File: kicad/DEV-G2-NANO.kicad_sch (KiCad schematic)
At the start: 0 parts

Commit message: added MIMXRT1171DVMAB symbol to project
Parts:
- added C1, C10, C11, C12, C13, C2, C3, C4, C5, C6: ???, symbol Device:C_Small
- added C14, C16, C17, C7, C8: 100nF, symbol Device:C_Small
- added C15: 1μF, symbol Device:C_Small
- added C9: 2.2μF, symbol Device:C_Small
- added D1, D2: ???, symbol Device:D_Small
- added J1: Micro_SD_Card, symbol Connector:Micro_SD_Card
- added J2: USB1, symbol Connector_Generic:Conn_01x04
- added L1: 4.7μH, symbol Device:L_Small
- added R1, R2, R3, R4: 10kΩ, symbol Device:R_Small_US
- added U1: MIMXRT1171DVMAB, symbol project_symbols:MIMXRT1171DVMAB
- added Y1: 24MHz, symbol Device:Crystal_Small
- added Y2: 32.768kHz, symbol Device:Crystal_Small
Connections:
- new net: C16.1, C9.1, U1.U11 (NVCC_SNVS), U1.U14 (VDD_SNVS_ANA)
- new net: C15.1, R1.1, U1.P3 (DCDC_PSWITCH)
- new net: R3.1, U1.F10 (VDD_MIPI_1P0)
- new net: C13.2, U1.U13 (RTC_XTALO), Y2.1
- new net: C12.2, U1.T13 (RTC_XTALI), Y2.2
- new net: D1.1 (K), D2.1 (K), U1.U12 (VDD_SNVS_IN)
- new net: J2.1 (Pin_1), U1.D17 (USB1_VBUS)
- new net: J2.2 (Pin_2), U1.E16 (USB1_DN)
- new net: J2.3 (Pin_3), U1.E17 (USB1_DP)
- new net: C11.2, U1.U16 (XTALI), Y1.1
- new net: C14.1, U1.P12 (VDD_LPSR_ANA)
- new net: J1.2 (DAT3/CD), U1.A16 (GPIO_SD_B1_05)
- new net: J1.1 (DAT2), U1.B15 (GPIO_SD_B1_04)
- new net: J1.3 (CMD), U1.B16 (GPIO_SD_B1_00)
- new net: J1.8 (DAT1), U1.B17 (GPIO_SD_B1_03)
- new net: J1.7 (DAT0), U1.C15 (GPIO_SD_B1_02)
- new net: J1.5 (CLK), U1.D15 (GPIO_SD_B1_01)
- new net: R2.1, U1.F9 (VDD_MIPI_1P8)
- new net: C7.1, U1.N11 (VDDA_1P0)
- new net: R4.1, U1.N4 (DCDC_MODE)
- new net: C8.1, U1.P11 (VDD_LPSR_DIG)
- new net: C17.1, U1.T14 (VDD_SNVS_DIG)
- new net: C10.2, U1.T16 (XTALO), Y1.2
- new net: L1.2, U1.T3 (DCDC_LP), U1.U3 (DCDC_LP)
- new net: L1.1, U1.T4 (DCDC_LN), U1.U4 (DCDC_LN)
- new net +1V0: C4.1, C5.1, C6.1, U1.H10 (VDD_SOC_IN), U1.H8 (VDD_SOC_IN), U1.H9 (VDD_SOC_IN), U1.J10 (VDD_SOC_IN), U1.J8 (VDD_SOC_IN), U1.J9 (VDD_SOC_IN), U1.K10 (VDD_SOC_IN), U1.K8 (DCDC_DIG), U1.K9 (DCDC_DIG), U1.L7 (DCDC_DIG_SENSE), U1.L8 (DCDC_DIG)
- new net +1V8: C1.1, C2.1, C3.1, U1.G16 (ADC_VREFH), U1.H12 (VDD_USB_1P8), U1.K15 (VDDA_ADC_1P8), U1.M11 (VDDA_1P8_IN), U1.M6 (DCDC_ANA_SENSE), U1.M7 (DCDC_ANA), U1.M8 (DCDC_ANA)
- new net +3V3: D1.2 (A), J1.4 (VDD), R1.2, U1.D12 (NVCC_DISP1), U1.D14 (NVCC_SD1), U1.E7 (NVCC_DISP2), U1.F6 (NVCC_EMC1), U1.F7 (NVCC_EMC1), U1.G12 (VDD_USB_3P3), U1.G13 (NVCC_SD2), U1.G6 (NVCC_EMC1), U1.H6 (NVCC_EMC2), U1.J13 (VDDA_ADC_3P3), U1.J6 (NVCC_EMC2), U1.L5 (DCDC_IN_Q), U1.M12 (NVCC_GPIO), U1.M5 (DCDC_IN), U1.N5 (DCDC_IN), U1.P7 (NVCC_LPSR), U1.R12 (VDD_LPSR_IN)
- new net GND: C1.2, C10.1, C11.1, C12.1, C13.1, C14.2, C15.2, C16.2, C17.2, C2.2, C3.2, C4.2, C5.2, C6.2, C7.2, C8.2, C9.2, J1.6 (VSS), J2.4 (Pin_4), R2.2, R3.2, R4.2, U1.A1 (VSS), U1.A17 (VSS), U1.B7 (VSS), U1.C10 (VSS), U1.C12 (VSS), U1.C14 (VSS), U1.C8 (VSS), U1.D4 (VSS), U1.F11 (VSS), U1.F12 (VSS), U1.F13 (VSS), U1.G10 (VSS), U1.G11 (VSS), U1.G15 (VSS), U1.G3 (VSS), U1.G7 (VSS), U1.G8 (VSS), U1.G9 (VSS), U1.H11 (VSS), U1.H7 (VSS), U1.J11 (VSS), U1.J7 (VSS), U1.K11 (VSS), U1.K6 (DCDC_GND), U1.K7 (DCDC_GND), U1.L10 (VSS), U1.L11 (VSS), U1.L15 (VSS), U1.L3 (VSS), U1.L6 (DCDC_GND), U1.P14 (VSS), U1.P4 (VSS), U1.R4 (VSS), U1.R7 (VSS), U1.T11 (TEST_MODE), U1.T12 (VSS), U1.U1 (VSS), U1.U17 (VSS)
- new net GNDA: J1.SH (SHIELD)
- new net POR_B: U1.T10 (POR_B)
- new net VBAT: D2.2 (A)
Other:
- added sheet Disclaimer (disclaimer.kicad_sch)
- note added: "Notes ----- * Since the POR_B pin needs 1.8V logic, it might make sense to power the MKL26Z128VFM4 at 1.8V. This would require setting the MIMXRT117x's UART bank to 1.8V as well..."
- note added: "Solder male header and use StarTech USBMBADAPT adapter (or similar)"
- note added: "TODO ---- 1. Review power sequence 2. Bypass capacitors 3. Where does VBAT come from? 4. GNDA needs coupling to GND"
- note added: "TODO: Where to route this 1.8V DAC?"
- note added: "\ | | \ TODO: / IMU & Magnetometer | | /"
- note added: "\ | | \ TODO: / RTMC Core | | /"
- note added: "\ | | \ TODO: / Wi-Fi Companion IC | | /"

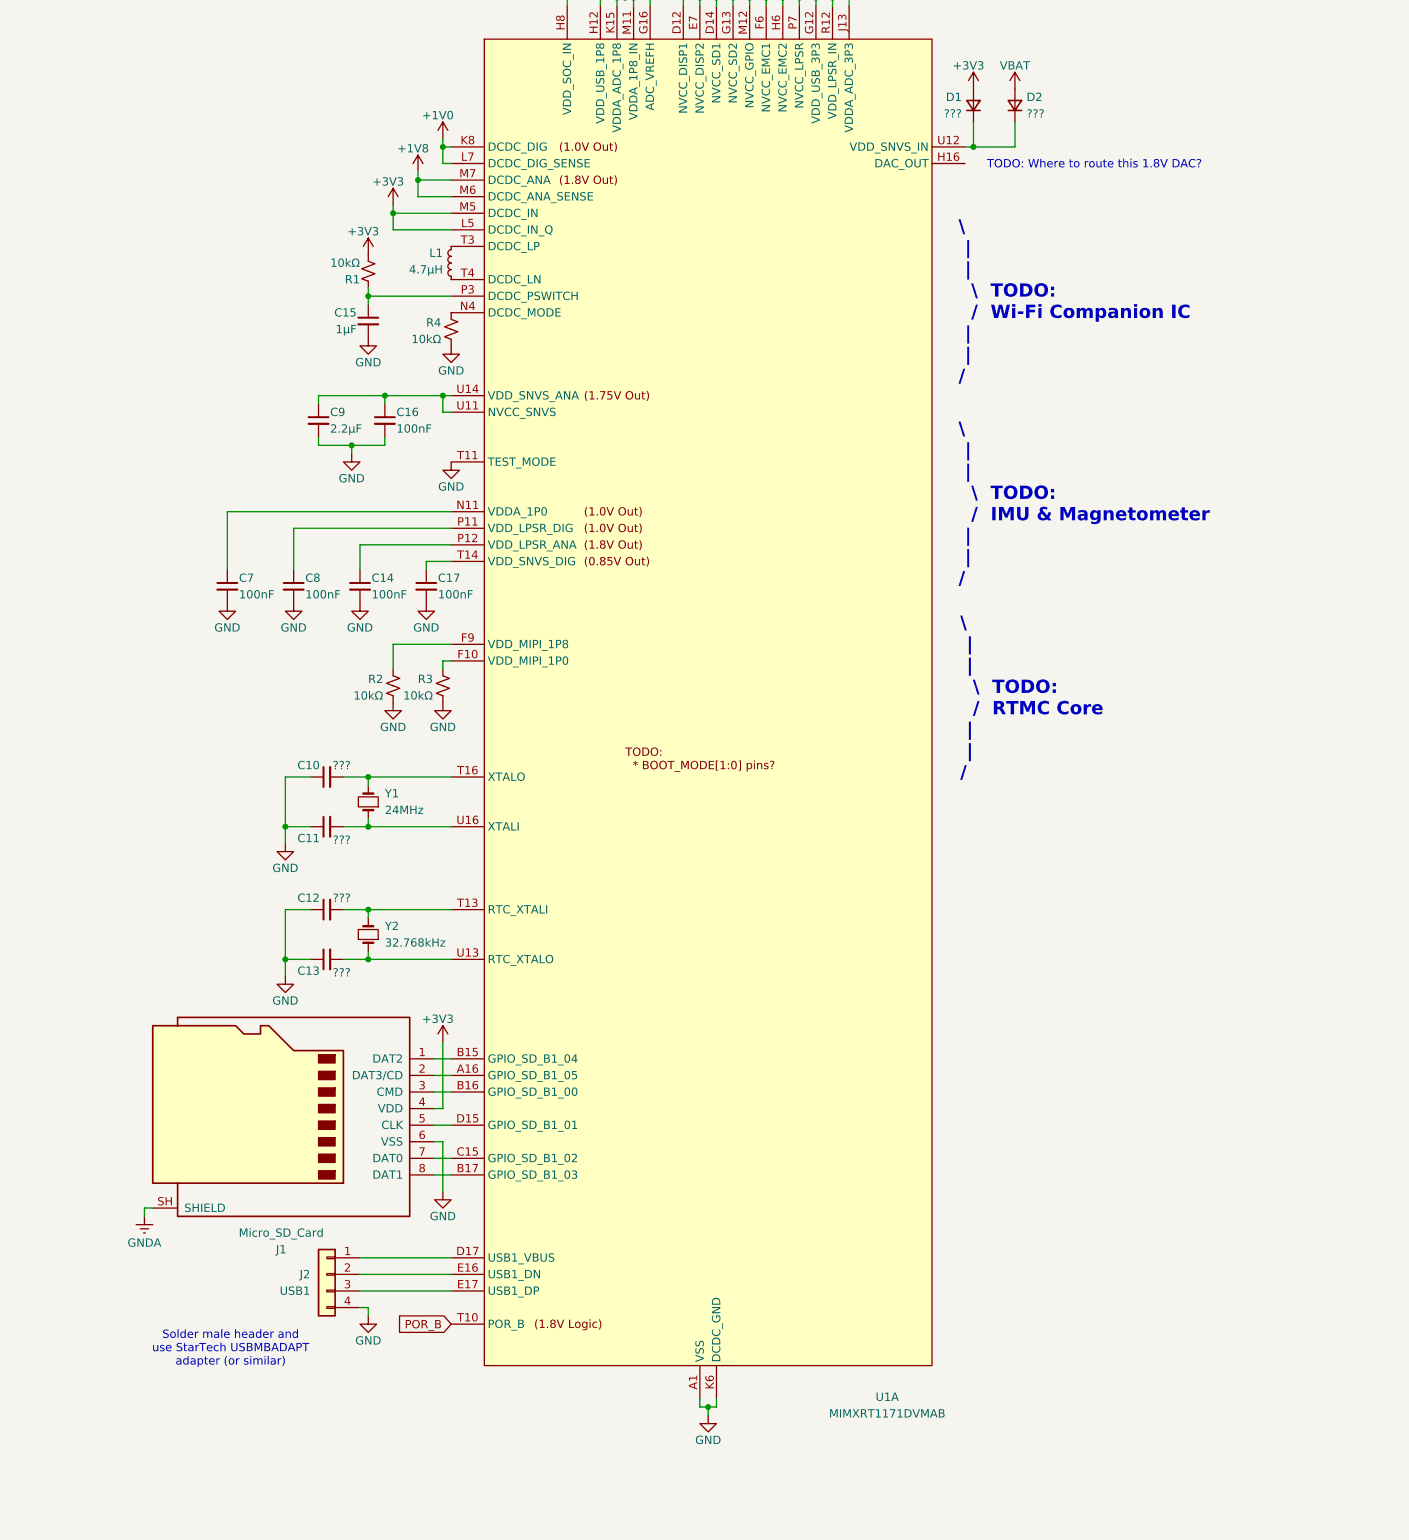
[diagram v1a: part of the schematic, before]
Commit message: added boot config and flash chip
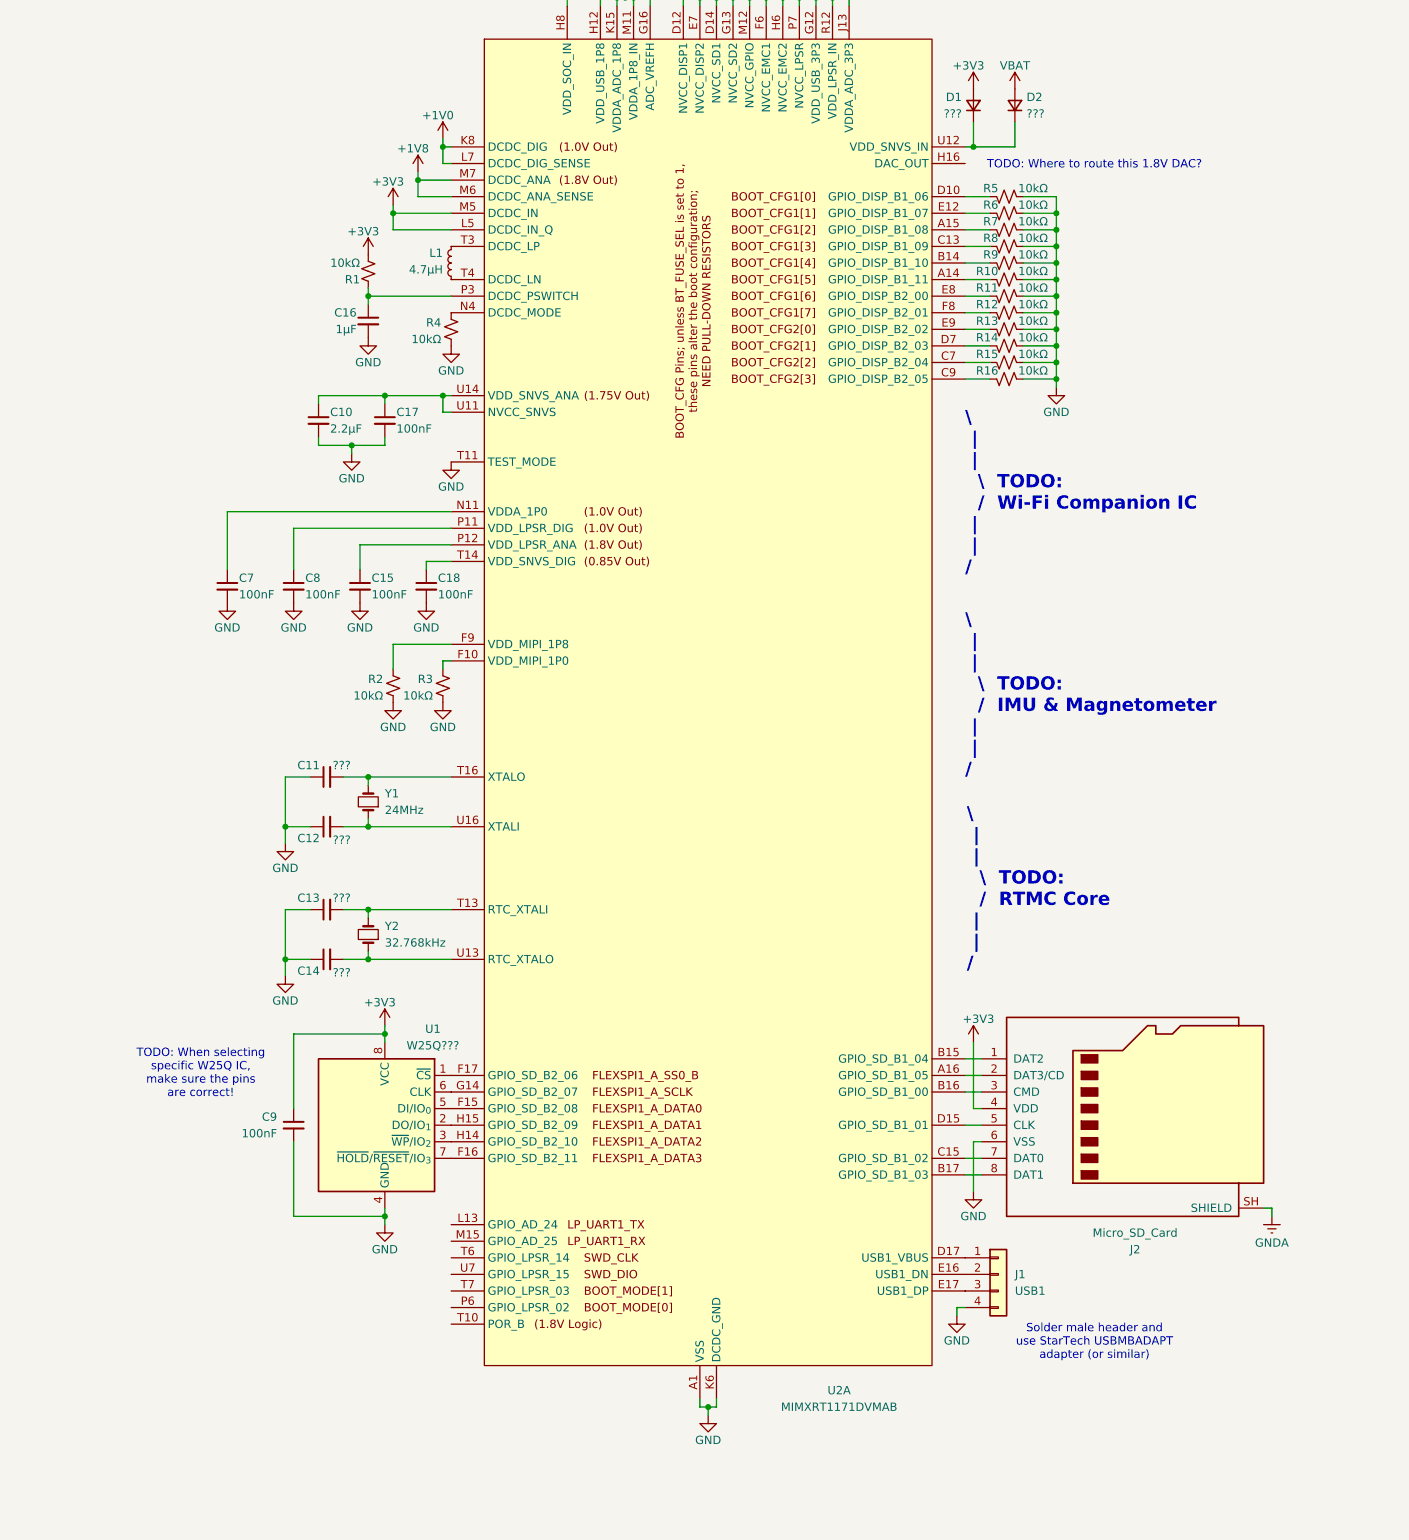
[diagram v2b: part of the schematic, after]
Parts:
- removed J1: Micro_SD_Card, symbol Connector:Micro_SD_Card
- removed J2: USB1, symbol Connector_Generic:Conn_01x04
- added C9: 100nF, symbol Device:C_Small
- added J1: USB1, symbol Connector_Generic:Conn_01x04
- added J2: Micro_SD_Card, symbol Connector:Micro_SD_Card
- added R10, R11, R12, R13, R14, R15, R16, R5, R6, R7, R8, R9: 10kΩ, symbol Device:R_Small_US
- added U1: W25Q???, symbol Memory_Flash:W25Q32JVSS
- renumbered C9 to C10, C10 to C11, C11 to C12, C12 to C13, C13 to C14, C14 to C15, C15 to C16, C16 to C17, C17 to C18, U1 to U2
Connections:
- net +3V3: now also C9.1, J2.4 (VDD), U1.8 (VCC)
- net GND: now also C9.2, J1.4 (Pin_4), J2.6 (VSS), R10.2, R11.2, R12.2, R13.2, R14.2, R15.2, R16.2, R5.2, R6.2, R7.2, R8.2, R9.2, U1.4 (GND)
- net GNDA: now also J2.SH (SHIELD)
- net at U2.D17 (USB1_VBUS): now also J1.1 (Pin_1)
- net at U2.E16 (USB1_DN): now also J1.2 (Pin_2)
- net at U2.E17 (USB1_DP): now also J1.3 (Pin_3)
- net at U2.A16 (GPIO_SD_B1_05): now also J2.2 (DAT3/CD)
- net at U2.B15 (GPIO_SD_B1_04): now also J2.1 (DAT2)
- net at U2.B16 (GPIO_SD_B1_00): now also J2.3 (CMD)
- net at U2.B17 (GPIO_SD_B1_03): now also J2.8 (DAT1)
- net at U2.C15 (GPIO_SD_B1_02): now also J2.7 (DAT0)
- net at U2.D15 (GPIO_SD_B1_01): now also J2.5 (CLK)
- net POR_B: no longer names the net of U2.T10 (POR_B)
- new net: R10.1, U2.A14 (GPIO_DISP_B1_11)
- new net: R12.1, U2.F8 (GPIO_DISP_B2_01)
- new net: R9.1, U2.B14 (GPIO_DISP_B1_10)
- new net: R7.1, U2.A15 (GPIO_DISP_B1_08)
- new net: R8.1, U2.C13 (GPIO_DISP_B1_09)
- new net: R15.1, U2.C7 (GPIO_DISP_B2_04)
- new net: R16.1, U2.C9 (GPIO_DISP_B2_05)
- new net: R5.1, U2.D10 (GPIO_DISP_B1_06)
- new net: R14.1, U2.D7 (GPIO_DISP_B2_03)
- new net: R6.1, U2.E12 (GPIO_DISP_B1_07)
- new net: R11.1, U2.E8 (GPIO_DISP_B2_00)
- new net: R13.1, U2.E9 (GPIO_DISP_B2_02)
- new net: U1.5 (DI/IO_{0}), U2.F15 (GPIO_SD_B2_08)
- new net: U1.7 (~{HOLD}/~{RESET}/IO_{3}), U2.F16 (GPIO_SD_B2_11)
- new net: U1.1 (~{CS}), U2.F17 (GPIO_SD_B2_06)
- new net: U1.6 (CLK), U2.G14 (GPIO_SD_B2_07)
- new net: U1.3 (~{WP}/IO_{2}), U2.H14 (GPIO_SD_B2_10)
- new net: U1.2 (DO/IO_{1}), U2.H15 (GPIO_SD_B2_09)
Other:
- note added: "TODO: When selecting specific W25Q IC, make sure the pins are correct!"

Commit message: broke up MIMXRT1171DVMAB into several units
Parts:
- removed C10: 2.2μF, symbol Device:C_Small
- removed C11, C12, C13, C14: ???, symbol Device:C_Small
- removed C15, C17, C18, C7, C8, C9: 100nF, symbol Device:C_Small
- removed C16: 1μF, symbol Device:C_Small
- removed D1, D2: ???, symbol Device:D_Small
- removed J1: USB1, symbol Connector_Generic:Conn_01x04
- removed J2: Micro_SD_Card, symbol Connector:Micro_SD_Card
- removed L1: 4.7μH, symbol Device:L_Small
- removed R1, R10, R11, R12, R13, R14, R15, R16, R2, R3, R4, R5, R6, R7, R8, R9: 10kΩ, symbol Device:R_Small_US
- removed U1: W25Q???, symbol Memory_Flash:W25Q32JVSS
- removed U2: MIMXRT1171DVMAB, symbol project_symbols:MIMXRT1171DVMAB
- removed Y1: 24MHz, symbol Device:Crystal_Small
- removed Y2: 32.768kHz, symbol Device:Crystal_Small
- added C19: 2.2μF, symbol Device:C_Small
- added C20: 1μF, symbol Device:C_Small
- added C21, C22, C23, C24, C25, C30: 100nF, symbol Device:C_Small
- added C26, C27, C28, C29: ???, symbol Device:C_Small
- added D3, D4: ???, symbol Device:D_Small
- added J3: Micro_SD_Card, symbol Connector:Micro_SD_Card
- added J4: USB1, symbol Connector_Generic:Conn_01x04
- added L2: 4.7μH, symbol Device:L_Small
- added R17, R18, R19, R20, R21, R22, R23, R24, R25, R26, R27, R28, R29, R30, R31, R32: 10kΩ, symbol Device:R_Small_US
- added U3: MIMXRT1171DVMAB, symbol project_symbols:MIMXRT1171DVMAB
- added U4: W25Q???, symbol Memory_Flash:W25Q32JVSS
- added Y3: 24MHz, symbol Device:Crystal_Small
- added Y4: 32.768kHz, symbol Device:Crystal_Small
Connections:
- net +1V0: now also U3.H10 (VDD_SOC_IN), U3.H8 (VDD_SOC_IN), U3.H9 (VDD_SOC_IN), U3.J10 (VDD_SOC_IN), U3.J8 (VDD_SOC_IN), U3.J9 (VDD_SOC_IN), U3.K10 (VDD_SOC_IN), U3.K8 (DCDC_DIG), U3.K9 (DCDC_DIG), U3.L7 (DCDC_DIG_SENSE), U3.L8 (DCDC_DIG)
- net +1V8: now also U3.G16 (ADC_VREFH), U3.H12 (VDD_USB_1P8), U3.K15 (VDDA_ADC_1P8), U3.M11 (VDDA_1P8_IN), U3.M6 (DCDC_ANA_SENSE), U3.M7 (DCDC_ANA), U3.M8 (DCDC_ANA)
- net +3V3: now also C30.1, D3.2 (A), J3.4 (VDD), R17.2, U3.D12 (NVCC_DISP1), U3.D14 (NVCC_SD1), U3.E7 (NVCC_DISP2), U3.F6 (NVCC_EMC1), U3.F7 (NVCC_EMC1), U3.G12 (VDD_USB_3P3), U3.G13 (NVCC_SD2), U3.G6 (NVCC_EMC1), U3.H6 (NVCC_EMC2), U3.J13 (VDDA_ADC_3P3), U3.J6 (NVCC_EMC2), U3.L5 (DCDC_IN_Q), U3.M12 (NVCC_GPIO), U3.M5 (DCDC_IN), U3.N5 (DCDC_IN), U3.P7 (NVCC_LPSR), U3.R12 (VDD_LPSR_IN), U4.8 (VCC)
- net GND: now also C19.2, C20.2, C21.2, C22.2, C23.2, C24.2, C25.2, C26.1, C27.1, C28.1, C29.1, C30.2, J3.6 (VSS), J4.4 (Pin_4), R18.2, R19.2, R20.2, R21.2, R22.2, R23.2, R24.2, R25.2, R26.2, R27.2, R28.2, R29.2, R30.2, R31.2, R32.2, U3.A1 (VSS), U3.A17 (VSS), U3.B7 (VSS), U3.C10 (VSS), U3.C12 (VSS), U3.C14 (VSS), U3.C8 (VSS), U3.D4 (VSS), U3.F11 (VSS), U3.F12 (VSS), U3.F13 (VSS), U3.G10 (VSS), U3.G11 (VSS), U3.G15 (VSS), U3.G3 (VSS), U3.G7 (VSS), U3.G8 (VSS), U3.G9 (VSS), U3.H11 (VSS), U3.H7 (VSS), U3.J11 (VSS), U3.J7 (VSS), U3.K11 (VSS), U3.K6 (DCDC_GND), U3.K7 (DCDC_GND), U3.L10 (VSS), U3.L11 (VSS), U3.L15 (VSS), U3.L3 (VSS), U3.L6 (DCDC_GND), U3.P14 (VSS), U3.P4 (VSS), U3.R4 (VSS), U3.R7 (VSS), U3.T11 (TEST_MODE), U3.T12 (VSS), U3.U1 (VSS), U3.U17 (VSS), U4.4 (GND)
- net GNDA: now also J3.SH (SHIELD)
- net VBAT: now also D4.2 (A)
- new net: R22.1, U3.E12 (GPIO_DISP_B1_07)
- new net: C22.1, U3.N11 (VDDA_1P0)
- new net: R20.1, U3.F10 (VDD_MIPI_1P0)
- new net: R19.1, U3.F9 (VDD_MIPI_1P8)
- new net: R18.1, U3.N4 (DCDC_MODE)
- new net: C23.1, U3.P11 (VDD_LPSR_DIG)
- new net: C24.1, U3.P12 (VDD_LPSR_ANA)
- new net: C20.1, R17.1, U3.P3 (DCDC_PSWITCH)
- new net: C28.2, U3.T13 (RTC_XTALI), Y4.2
- new net: C25.1, U3.T14 (VDD_SNVS_DIG)
- new net: C26.2, U3.T16 (XTALO), Y3.2
- new net: L2.2, U3.T3 (DCDC_LP), U3.U3 (DCDC_LP)
- new net: L2.1, U3.T4 (DCDC_LN), U3.U4 (DCDC_LN)
- new net: C19.1, C21.1, U3.U11 (NVCC_SNVS), U3.U14 (VDD_SNVS_ANA)
- new net: D3.1 (K), D4.1 (K), U3.U12 (VDD_SNVS_IN)
- new net: C29.2, U3.U13 (RTC_XTALO), Y4.1
- new net: C27.2, U3.U16 (XTALI), Y3.1
- new net: R32.1, U3.C9 (GPIO_DISP_B2_05)
- new net: R25.1, U3.B14 (GPIO_DISP_B1_10)
- new net: U3.F17 (GPIO_SD_B2_06), U4.1 (~{CS})
- new net: U3.H15 (GPIO_SD_B2_09), U4.2 (DO/IO_{1})
- new net: U3.H14 (GPIO_SD_B2_10), U4.3 (~{WP}/IO_{2})
- new net: U3.F15 (GPIO_SD_B2_08), U4.5 (DI/IO_{0})
- new net: U3.G14 (GPIO_SD_B2_07), U4.6 (CLK)
- new net: U3.F16 (GPIO_SD_B2_11), U4.7 (~{HOLD}/~{RESET}/IO_{3})
- new net: J4.1 (Pin_1), U3.D17 (USB1_VBUS)
- new net: J4.2 (Pin_2), U3.E16 (USB1_DN)
- new net: J4.3 (Pin_3), U3.E17 (USB1_DP)
- new net: R27.1, U3.E8 (GPIO_DISP_B2_00)
- new net: R29.1, U3.E9 (GPIO_DISP_B2_02)
- new net: R26.1, U3.A14 (GPIO_DISP_B1_11)
- new net: R30.1, U3.D7 (GPIO_DISP_B2_03)
- new net: R31.1, U3.C7 (GPIO_DISP_B2_04)
- new net: R21.1, U3.D10 (GPIO_DISP_B1_06)
- new net: R24.1, U3.C13 (GPIO_DISP_B1_09)
- new net: R23.1, U3.A15 (GPIO_DISP_B1_08)
- new net: R28.1, U3.F8 (GPIO_DISP_B2_01)
- new net: J3.2 (DAT3/CD), U3.A16 (GPIO_SD_B1_05)
- new net: J3.1 (DAT2), U3.B15 (GPIO_SD_B1_04)
- new net: J3.3 (CMD), U3.B16 (GPIO_SD_B1_00)
- new net: J3.8 (DAT1), U3.B17 (GPIO_SD_B1_03)
- new net: J3.7 (DAT0), U3.C15 (GPIO_SD_B1_02)
- new net: J3.5 (CLK), U3.D15 (GPIO_SD_B1_01)
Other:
- note removed: "\ | | \ TODO: / IMU & Magnetometer | | /"
- note removed: "\ | | \ TODO: / RTMC Core | | /"
- note removed: "\ | | \ TODO: / Wi-Fi Companion IC | | /"
- moved on the sheet: C1, C2, C3, C4, C5, C6

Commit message: organized schematic into several sheets
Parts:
- removed C1, C2, C26, C27, C28, C29, C3, C4, C5, C6: ???, symbol Device:C_Small
- removed C19: 2.2μF, symbol Device:C_Small
- removed C20: 1μF, symbol Device:C_Small
- removed C21, C22, C23, C24, C25, C30: 100nF, symbol Device:C_Small
- removed D3, D4: ???, symbol Device:D_Small
- removed J3: Micro_SD_Card, symbol Connector:Micro_SD_Card
- removed J4: USB1, symbol Connector_Generic:Conn_01x04
- removed L2: 4.7μH, symbol Device:L_Small
- removed R17, R18, R19, R20, R21, R22, R23, R24, R25, R26, R27, R28, R29, R30, R31, R32: 10kΩ, symbol Device:R_Small_US
- removed U3: MIMXRT1171DVMAB, symbol project_symbols:MIMXRT1171DVMAB
- removed U4: W25Q???, symbol Memory_Flash:W25Q32JVSS
- removed Y3: 24MHz, symbol Device:Crystal_Small
- removed Y4: 32.768kHz, symbol Device:Crystal_Small
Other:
- removed sheet Disclaimer
- added sheet Configuration (configuration.kicad_sch)
- added sheet Power (power.kicad_sch)
- added sheet User IO (user-io.kicad_sch)
- note added: "DEV-G2-NANO Development Board"
- note added: "Revision History"
- note removed: "Notes ----- * Since the POR_B pin needs 1.8V logic, it might make sense to power the MKL26Z128VFM4 at 1.8V. This would require setting the MIMXRT117x's UART bank to 1.8V as well..."
- note removed: "Solder male header and use StarTech USBMBADAPT adapter (or similar)"
- note removed: "TODO ---- 1. Review power sequence 2. Bypass capacitors 3. Where does VBAT come from? 4. GNDA needs coupling to GND"
- note removed: "TODO: When selecting specific W25Q IC, make sure the pins are correct!"
- note removed: "TODO: Where to route this 1.8V DAC?"
